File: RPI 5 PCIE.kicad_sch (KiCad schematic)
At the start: 1 part, among them J1 Conn_01x16

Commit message: Created Schematic
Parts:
- added J2: ATX-24, symbol Connector:ATX-24
- added PCIe_x16: ~, symbol PCIE:PCIE_x16_Unamed_Pins
- added Q1: MMBT3904, Package_TO_SOT_SMD:SOT-23, symbol Transistor_BJT:MMBT3904
- added R1: 4.7k, symbol Device:R_US
- added R2: 2.2k, symbol Device:R_US
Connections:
- net at J1.10 (Pin_10): now also PCIe_x16.14 (B)
- net at J1.11 (Pin_11): now also PCIe_x16.15 (B)
- net GND: now reaches J1.12 (Pin_12)
- net GND: now also J1.3 (Pin_3), J1.6 (Pin_6), J1.9 (Pin_9), PCIe_x16.13 (B), PCIe_x16.15 (B), PCIe_x16.16 (B), PCIe_x16.18 (B), PCIe_x16.21 (B), PCIe_x16.22 (B), PCIe_x16.23 (B), PCIe_x16.24 (B), PCIe_x16.25 (B), PCIe_x16.26 (B), PCIe_x16.27 (B), PCIe_x16.28 (B), PCIe_x16.29 (B), PCIe_x16.31 (B), PCIe_x16.32 (B), PCIe_x16.34 (B), PCIe_x16.35 (B), PCIe_x16.36 (B), PCIe_x16.37 (B), PCIe_x16.38 (B), PCIe_x16.39 (B), PCIe_x16.4 (B), PCIe_x16.40 (B), PCIe_x16.41 (B), PCIe_x16.42 (B), PCIe_x16.43 (B), PCIe_x16.44 (B), PCIe_x16.45 (B), PCIe_x16.46 (B), PCIe_x16.47 (B), PCIe_x16.49 (B), PCIe_x16.51 (B), PCIe_x16.52 (B), PCIe_x16.53 (B), PCIe_x16.54 (B), PCIe_x16.55 (B), PCIe_x16.56 (B), PCIe_x16.57 (B), PCIe_x16.58 (B), PCIe_x16.59 (B), PCIe_x16.60 (B), PCIe_x16.61 (B), PCIe_x16.62 (B), PCIe_x16.63 (B), PCIe_x16.64 (B), PCIe_x16.65 (B), PCIe_x16.66 (B), PCIe_x16.67 (B), PCIe_x16.68 (B), PCIe_x16.69 (B), PCIe_x16.7 (B), PCIe_x16.70 (B), PCIe_x16.71 (B), PCIe_x16.72 (B), PCIe_x16.73 (B), PCIe_x16.74 (B), PCIe_x16.75 (B), PCIe_x16.76 (B), PCIe_x16.77 (B), PCIe_x16.78 (B), PCIe_x16.79 (B), PCIe_x16.80 (B), PCIe_x16.82 (B), Q1.2 (E)
- net at J1.13 (Pin_13): now also R1.1
- net at J1.14 (Pin_14): now also R2.2
- net at J1.15 (Pin_15): now also PCIe_x16.12 (B)
- net at J1.16 (Pin_16): now also PCIe_x16.11 (B)
- net at J1.4 (Pin_4): now also PCIe_x16.13 (B)
- net at J1.5 (Pin_5): now also PCIe_x16.14 (B)
- net at J1.7 (Pin_7): now also PCIe_x16.16 (B)
- net at J1.8 (Pin_8): now also PCIe_x16.17 (B)
- new net: Q1.1 (B), R1.2
- new net: J2.16 (PS_ON#), Q1.3 (C)
- new net: J2.15 (GND), J2.17 (GND), J2.18 (GND), J2.19 (GND), J2.24 (GND), J2.3 (GND), J2.5 (GND), J2.7 (GND)
- new net: J2.21 (+5V), J2.22 (+5V), J2.23 (+5V), J2.4 (+5V), J2.6 (+5V)
- new net +12V: J2.10 (+12V), J2.11 (+12V), PCIe_x16.1 (B), PCIe_x16.2 (B), PCIe_x16.3 (B)
- new net +3.3V: J2.1 (+3.3V), J2.12 (+3.3V), J2.13 (+3.3V), J2.2 (+3.3V), PCIe_x16.10 (B), PCIe_x16.5 (B), PCIe_x16.6 (B), PCIe_x16.8 (B), PCIe_x16.9 (B), R2.1
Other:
- moved on the sheet: J1

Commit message: Started PCB
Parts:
- J1: footprint (none) -> MyConnectors:Cvilux_CF31161D0R0-05-NH
- J2: footprint (none) -> Connector_Molex:Molex_Mini-Fit_Jr_5566-24A2_2x12_P4.20mm_Vertical
- PCIe_x16: footprint (none) -> PCIe:PCIe x16
- R1, R2: footprint (none) -> Resistor_SMD:R_1206_3216Metric
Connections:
- net +12V: now also PCIe_x16.A2, PCIe_x16.A3, PCIe_x16.B1, PCIe_x16.B2, PCIe_x16.B3; no longer PCIe_x16.1 (B), PCIe_x16.2 (B), PCIe_x16.3 (B)
- net +3.3V: now also PCIe_x16.A10, PCIe_x16.A5, PCIe_x16.A6, PCIe_x16.A8, PCIe_x16.A9, PCIe_x16.B10, PCIe_x16.B8, PCIe_x16.B9; no longer PCIe_x16.10 (B), PCIe_x16.5 (B), PCIe_x16.6 (B), PCIe_x16.8 (B), PCIe_x16.9 (B)
- net GND: now also J2.15 (GND), J2.17 (GND), J2.18 (GND), J2.19 (GND), J2.24 (GND), J2.3 (GND), J2.5 (GND), J2.7 (GND), PCIe_x16.A15, PCIe_x16.A18, PCIe_x16.A20, PCIe_x16.A23, PCIe_x16.A24, PCIe_x16.A27, PCIe_x16.A28, PCIe_x16.A31, PCIe_x16.A34, PCIe_x16.A37, PCIe_x16.A38, PCIe_x16.A4, PCIe_x16.A41, PCIe_x16.A42, PCIe_x16.A45, PCIe_x16.A46, PCIe_x16.A49, PCIe_x16.A51, PCIe_x16.A54, PCIe_x16.A55, PCIe_x16.A58, PCIe_x16.A59, PCIe_x16.A62, PCIe_x16.A63, PCIe_x16.A66, PCIe_x16.A67, PCIe_x16.A70, PCIe_x16.A71, PCIe_x16.A74, PCIe_x16.A75, PCIe_x16.A78, PCIe_x16.A79, PCIe_x16.A82, PCIe_x16.B13, PCIe_x16.B16, PCIe_x16.B18, PCIe_x16.B21, PCIe_x16.B22, PCIe_x16.B25, PCIe_x16.B26, PCIe_x16.B29, PCIe_x16.B32, PCIe_x16.B35, PCIe_x16.B36, PCIe_x16.B39, PCIe_x16.B4, PCIe_x16.B40, PCIe_x16.B43, PCIe_x16.B44, PCIe_x16.B47, PCIe_x16.B49, PCIe_x16.B52, PCIe_x16.B53, PCIe_x16.B56, PCIe_x16.B57, PCIe_x16.B60, PCIe_x16.B61, PCIe_x16.B64, PCIe_x16.B65, PCIe_x16.B68, PCIe_x16.B69, PCIe_x16.B7, PCIe_x16.B72, PCIe_x16.B73, PCIe_x16.B76, PCIe_x16.B77, PCIe_x16.B80; no longer PCIe_x16.13 (B), PCIe_x16.15 (B), PCIe_x16.16 (B), PCIe_x16.18 (B), PCIe_x16.21 (B), PCIe_x16.22 (B), PCIe_x16.23 (B), PCIe_x16.24 (B), PCIe_x16.25 (B), PCIe_x16.26 (B), PCIe_x16.27 (B), PCIe_x16.28 (B), PCIe_x16.29 (B), PCIe_x16.31 (B), PCIe_x16.32 (B), PCIe_x16.34 (B), PCIe_x16.35 (B), PCIe_x16.36 (B), PCIe_x16.37 (B), PCIe_x16.38 (B), PCIe_x16.39 (B), PCIe_x16.4 (B), PCIe_x16.40 (B), PCIe_x16.41 (B), PCIe_x16.42 (B), PCIe_x16.43 (B), PCIe_x16.44 (B), PCIe_x16.45 (B), PCIe_x16.46 (B), PCIe_x16.47 (B), PCIe_x16.49 (B), PCIe_x16.51 (B), PCIe_x16.52 (B), PCIe_x16.53 (B), PCIe_x16.54 (B), PCIe_x16.55 (B), PCIe_x16.56 (B), PCIe_x16.57 (B), PCIe_x16.58 (B), PCIe_x16.59 (B), PCIe_x16.60 (B), PCIe_x16.61 (B), PCIe_x16.62 (B), PCIe_x16.63 (B), PCIe_x16.64 (B), PCIe_x16.65 (B), PCIe_x16.66 (B), PCIe_x16.67 (B), PCIe_x16.68 (B), PCIe_x16.69 (B), PCIe_x16.7 (B), PCIe_x16.70 (B), PCIe_x16.71 (B), PCIe_x16.72 (B), PCIe_x16.73 (B), PCIe_x16.74 (B), PCIe_x16.75 (B), PCIe_x16.76 (B), PCIe_x16.77 (B), PCIe_x16.78 (B), PCIe_x16.79 (B), PCIe_x16.80 (B), PCIe_x16.82 (B)
- net at J1.10 (Pin_10): now also PCIe_x16.B14; no longer PCIe_x16.14 (B)
- net at J1.11 (Pin_11): now also PCIe_x16.B15; no longer PCIe_x16.15 (B)
- net at J1.15 (Pin_15): now also PCIe_x16.B12; no longer PCIe_x16.12 (B)
- net at J1.16 (Pin_16): now also PCIe_x16.A11; no longer PCIe_x16.11 (B)
- net at J1.4 (Pin_4): now also PCIe_x16.A13; no longer PCIe_x16.13 (B)
- net at J1.5 (Pin_5): now also PCIe_x16.A14; no longer PCIe_x16.14 (B)
- net at J1.7 (Pin_7): now also PCIe_x16.A16; no longer PCIe_x16.16 (B)
- net at J1.8 (Pin_8): now also PCIe_x16.A17; no longer PCIe_x16.17 (B)
- no-connect marks 0 -> 82

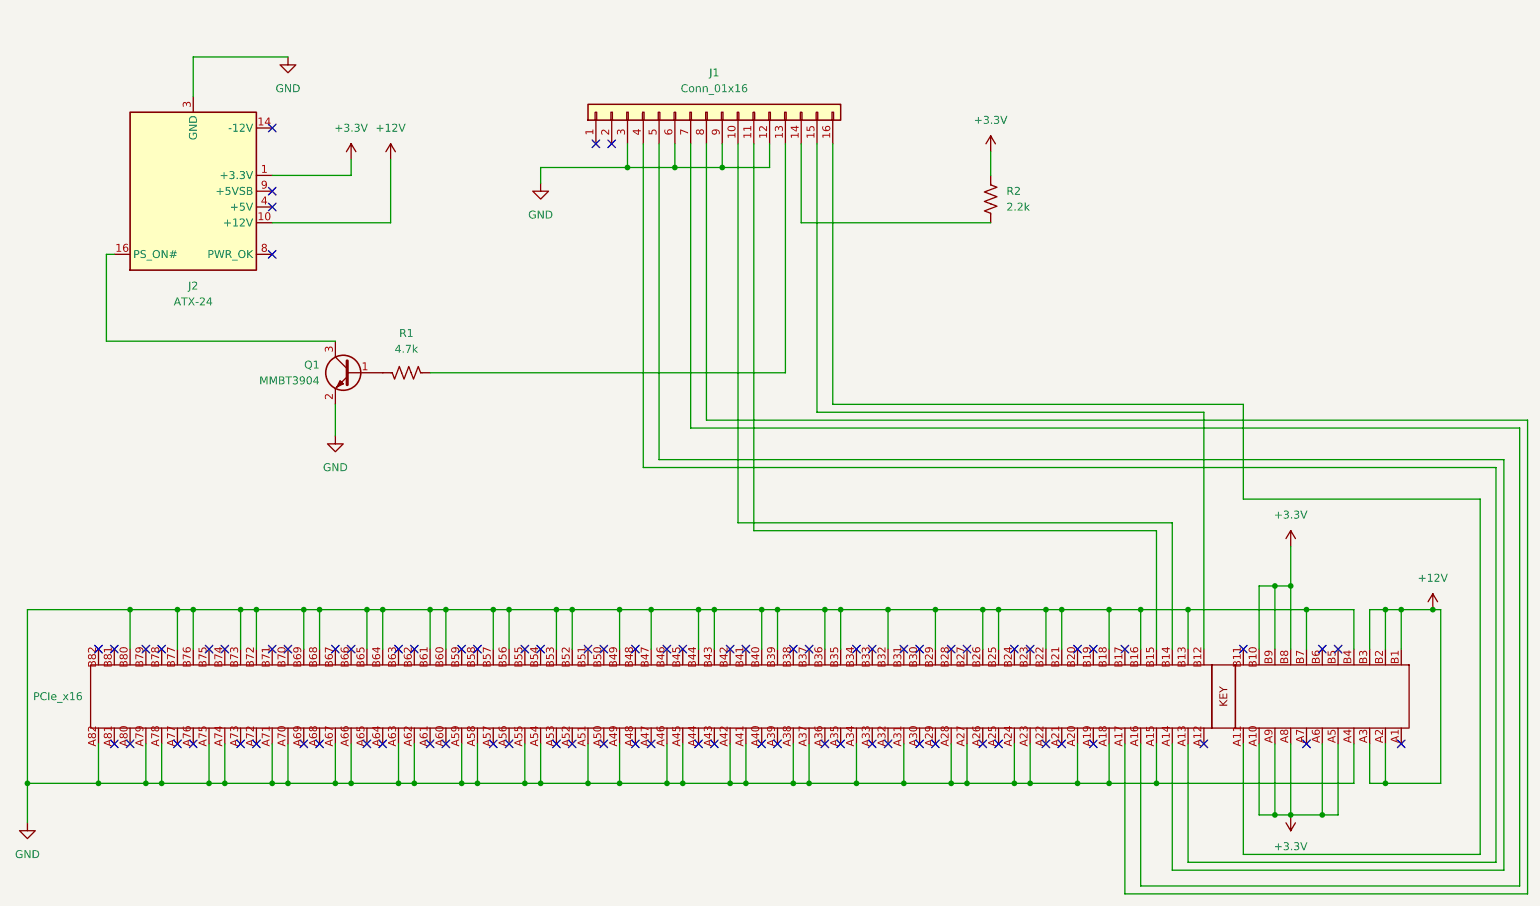
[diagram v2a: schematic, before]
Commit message: Attempted PCB Design
Realized that a 4-layer PCB is required. Will continue research into impedance controlled PCBs
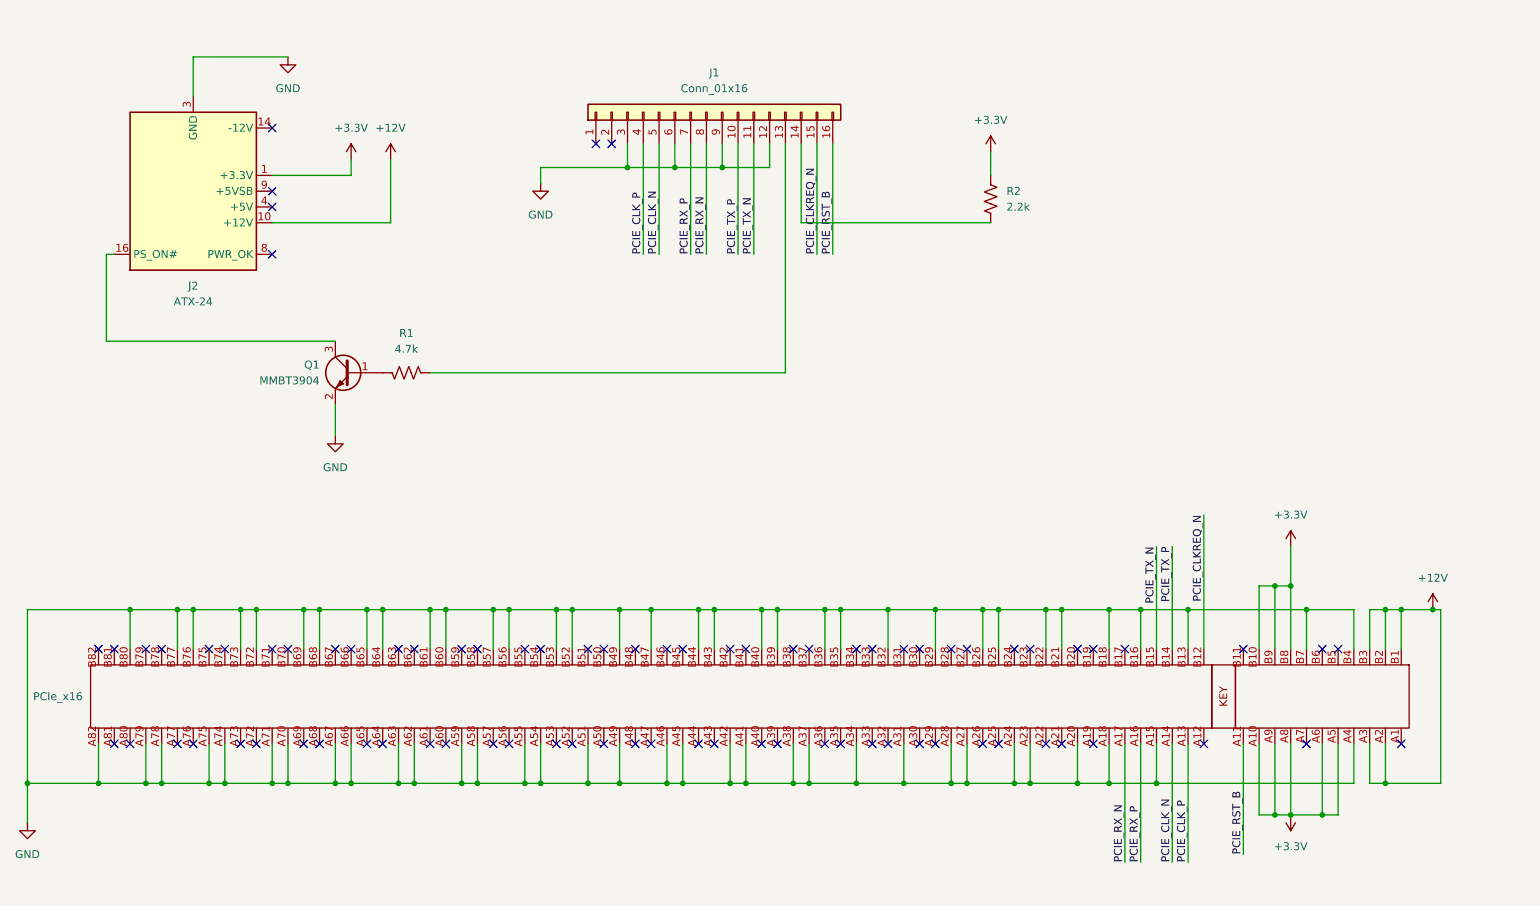
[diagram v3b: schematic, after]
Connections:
- net PCIE_TX_P: now reaches J1.10 (Pin_10), PCIe_x16.B14
- net PCIE_TX_N: now reaches J1.11 (Pin_11), PCIe_x16.B15
- net PCIE_CLKREQ_N: now reaches J1.15 (Pin_15), PCIe_x16.B12
- net PCIE_RST_B: now reaches J1.16 (Pin_16), PCIe_x16.A11
- net PCIE_CLK_P: now reaches J1.4 (Pin_4), PCIe_x16.A13
- net PCIE_CLK_N: now reaches J1.5 (Pin_5), PCIe_x16.A14
- net PCIE_RX_P: now reaches J1.7 (Pin_7), PCIe_x16.A16
- net PCIE_RX_N: now reaches J1.8 (Pin_8), PCIe_x16.A17

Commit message: Finished PCB v1
This was the first prototype to be sent to JLC PCB
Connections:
- net PCIE_TX_N: now also J1.10 (Pin_10); no longer J1.11 (Pin_11)
- net PCIE_TX_P: now also J1.11 (Pin_11); no longer J1.10 (Pin_10)
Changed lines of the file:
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@@
     (stroke (width 0) (type default))
+  )
+  (text_box "Swaped PCIE TX + and - for easier PCB routing"
+    (at 128.27 29.21 0) (size 16.51 7.62)
+    (stroke (width -0.0001) (type default))
+    (fill (type none))
+    (effects (font (size 1.27 1.27)) (justify left top))
   )
   (label "PCIE_RX_P" (at 128.27 68.58 90) (fields_autoplaced)
@@
     (effects (font (size 1.27 1.27)) (justify left bottom))
   )
-  (label "PCIE_TX_P" (at 135.89 68.58 90) (fields_autoplaced)
+  (label "PCIE_TX_P" (at 138.43 68.58 90) (fields_autoplaced)
     (effects (font (size 1.27 1.27)) (justify left bottom))
   )
@@
     (effects (font (size 1.27 1.27)) (justify right bottom))
   )
-  (label "PCIE_TX_N" (at 138.43 68.58 90) (fields_autoplaced)
+  (label "PCIE_TX_N" (at 135.89 68.58 90) (fields_autoplaced)
     (effects (font (size 1.27 1.27)) (justify left bottom))
   )
